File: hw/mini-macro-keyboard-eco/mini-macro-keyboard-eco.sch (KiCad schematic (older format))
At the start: 28 parts, among them J0 USB, J1 DEBUG_SWD, SW1 SW_Cherry_MX_1.00u_PCB, SW2 SW_Cherry_MX_1.00u_PCB, SW3 SW_Cherry_MX_1.00u_PCB, SW5 LAYOUT, SW6 BACKLIGHT, U1 USBLC6-2SC6, U2 XC6206P322MR, U3 STM32F070F6P6, Y1 16 MHz

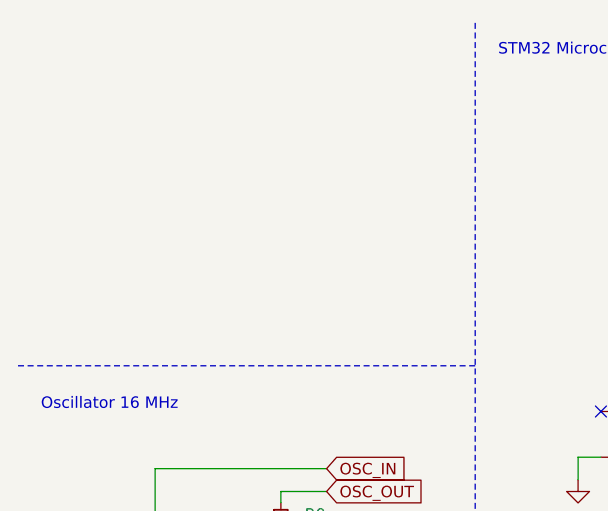
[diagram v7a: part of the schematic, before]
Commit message: feat(hw): add mounting holes
Signed-off-by: Ivan Kovalenko <s1ckretbox@gmail.com>
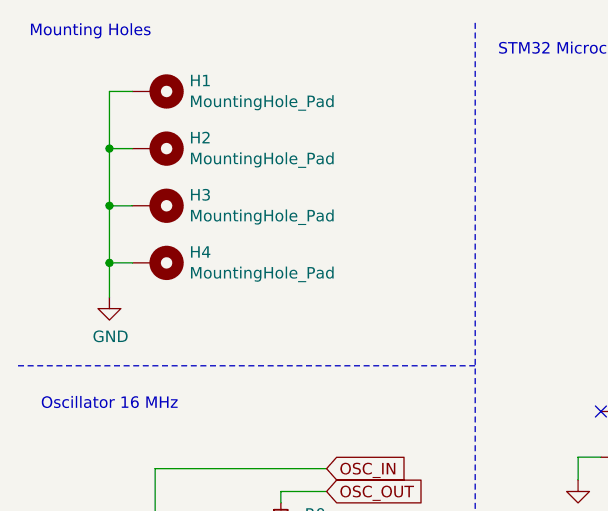
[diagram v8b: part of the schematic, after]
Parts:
- added H1, H2, H3, H4: MountingHole_Pad, MountingHole:MountingHole_2.2mm_M2_ISO7380_Pad, symbol Mechanical:MountingHole_Pad
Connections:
- net GND: now also H1.1, H2.1, H3.1, H4.1
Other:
- note added: "Mounting Holes\n\n"
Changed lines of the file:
@@
 Wire Notes Line
 	2500 2000 500  2000
+Text Notes 550  650  0    50   ~ 0
+Mounting Holes\n\n
+$Comp
+L Mechanical:MountingHole_Pad H1
+U 1 1 60158ED2
+P 1100 800
+F 0 "H1" V 1054 950 50  0000 L CNN
+F 1 "MountingHole_Pad" V 1145 950 50  0000 L CNN
+F 2 "MountingHole:MountingHole_2.2mm_M2_ISO7380_Pad" H 1100 800 50  0001 C CNN
+F 3 "~" H 1100 800 50  0001 C CNN
+	1    1100 800
+	0    1    1    0
+$EndComp
+$Comp
+L Mechanical:MountingHole_Pad H2
+U 1 1 6015B489
+P 1100 1050
+F 0 "H2" V 1054 1200 50  0000 L CNN
+F 1 "MountingHole_Pad" V 1145 1200 50  0000 L CNN
+F 2 "MountingHole:MountingHole_2.2mm_M2_ISO7380_Pad" H 1100 1050 50  0001 C CNN
+F 3 "~" H 1100 1050 50  0001 C CNN
+	1    1100 1050
+	0    1    1    0
+$EndComp
+$Comp
+L Mechanical:MountingHole_Pad H3
+U 1 1 6015BA51
+P 1100 1300
+F 0 "H3" V 1054 1450 50  0000 L CNN
+F 1 "MountingHole_Pad" V 1145 1450 50  0000 L CNN
+F 2 "MountingHole:MountingHole_2.2mm_M2_ISO7380_Pad" H 1100 1300 50  0001 C CNN
+F 3 "~" H 1100 1300 50  0001 C CNN
+	1    1100 1300
+	0    1    1    0
+$EndComp
+$Comp
+L Mechanical:MountingHole_Pad H4
+U 1 1 6015BDD9
+P 1100 1550
+F 0 "H4" V 1054 1700 50  0000 L CNN
+F 1 "MountingHole_Pad" V 1145 1700 50  0000 L CNN
+F 2 "MountingHole:MountingHole_2.2mm_M2_ISO7380_Pad" H 1100 1550 50  0001 C CNN
+F 3 "~" H 1100 1550 50  0001 C CNN
+	1    1100 1550
+	0    1    1    0
+$EndComp
+$Comp
+L mini-macro-keyboard-eco-rescue:GND-power #PWR06
+U 1 1 6015E4B8
+P 900 1700
+F 0 "#PWR06" H 900 1450 50  0001 C CNN
+F 1 "GND" H 905 1527 50  0000 C CNN
+F 2 "" H 900 1700 50  0001 C CNN
+F 3 "" H 900 1700 50  0001 C CNN
+	1    900  1700
+	1    0    0    -1
+$EndComp
+Wire Wire Line
+	1000 800  900  800
+Wire Wire Line
+	900  800  900  1050
+Wire Wire Line
+	1000 1550 900  1550
+Connection ~ 900  1550
+Wire Wire Line
+	900  1550 900  1700
+Wire Wire Line
+	900  1300 1000 1300
+Connection ~ 900  1300
+Wire Wire Line
+	900  1300 900  1550
+Wire Wire Line
+	1000 1050 900  1050
+Connection ~ 900  1050
+Wire Wire Line
+	900  1050 900  1300
 $EndSCHEMATC
